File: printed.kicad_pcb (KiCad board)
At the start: 2 copper layers, 20.1 x 20.1 mm, 4 parts

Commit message: Netlist
Correctly Generated the letlist
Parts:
- removed 5050-2812B (x4): LED***, WS2812B
- added LED1: WS2812B, WS2812B, F.Cu at (162.6, 87.6)
- added LED2: WS2812B, WS2812B, F.Cu at (162.6, 95.2)
- added LED3: WS2812B, WS2812B, F.Cu at (170.2, 87.6)
- added LED4: WS2812B, WS2812B, F.Cu at (170.2, 95.2)
- added P1: CONN_4, 4P-Header, F.Cu at (160.0, 87.6)
- added P2: CONN_4, 4P-Header, F.Cu at (177.8, 87.6)
- added SIL-4: Val**, SIL-4, F.Cu at (0.00, 0.00)

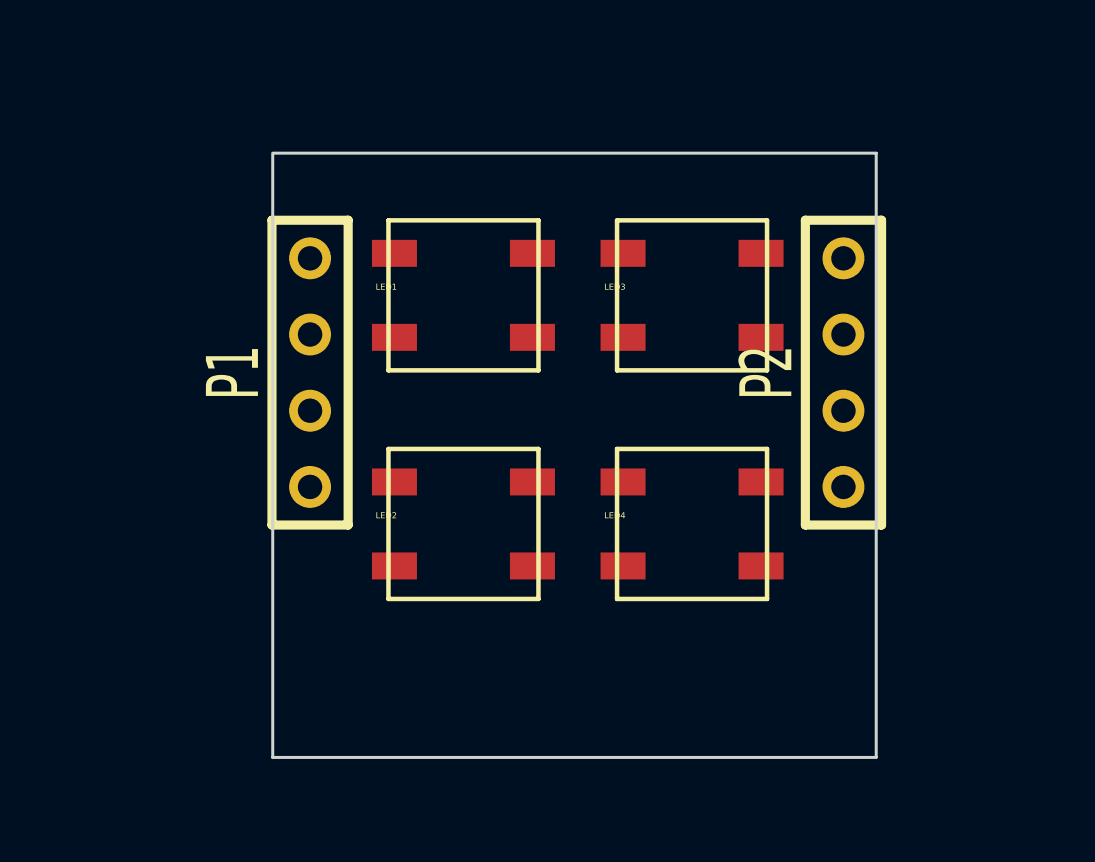
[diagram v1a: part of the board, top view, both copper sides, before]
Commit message: ws2812b schematic file
missed exporting the file
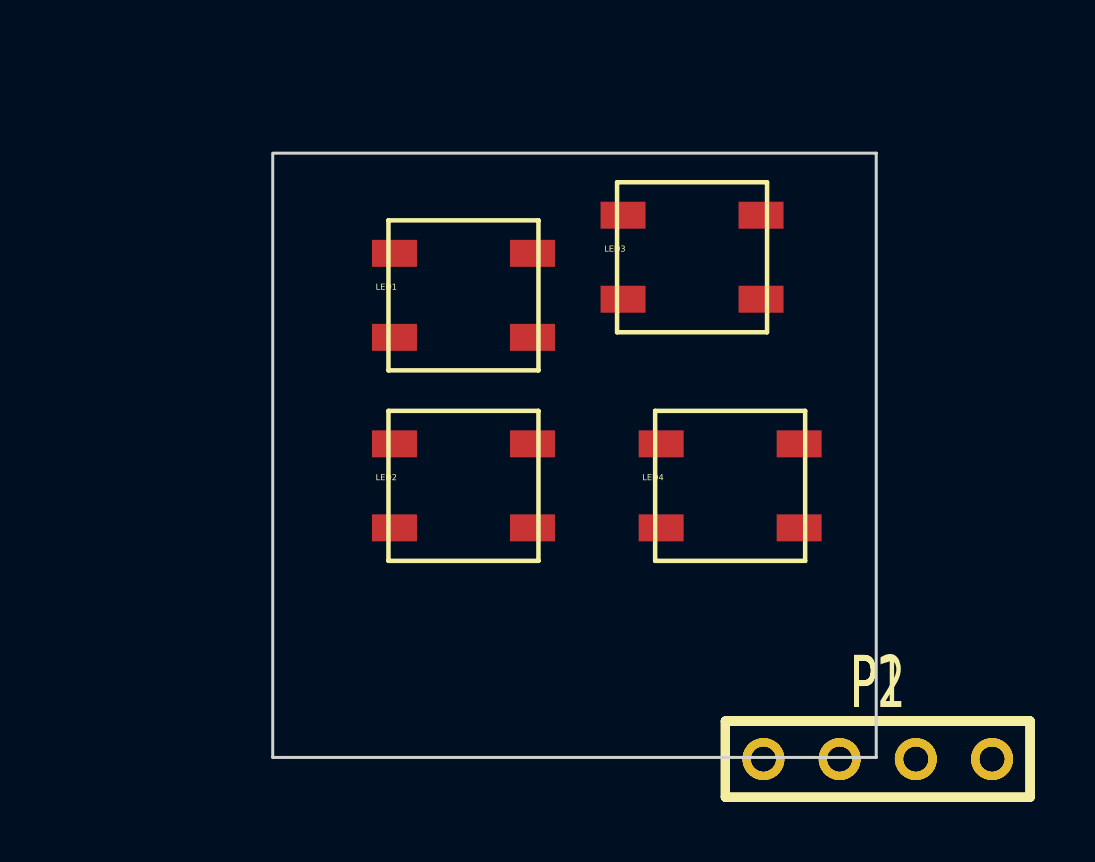
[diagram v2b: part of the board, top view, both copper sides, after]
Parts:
- moved P1 22.9 mm to (178.9, 100.5), turned to 0 degrees
- moved P2 12.9 mm to (178.9, 100.5), turned to 0 degrees
- moved LED4 1.80 mm to (171.4, 94.0)
- moved LED2 1.27 mm to (162.6, 94.0)
- moved LED3 1.27 mm to (170.2, 86.4)
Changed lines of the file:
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@@
   )
   (module WS2812B (layer Front.Layer)
-    (at 170.18 87.63)
+    (at 170.18 86.36)
     (descr "SMT 5050 WD2812")
     (fp_text reference LED3 (at 0 -2.8575) (layer F.SilkS)
@@
   )
   (module WS2812B (layer Front.Layer)
-    (at 162.56 95.25)
+    (at 162.56 93.98)
     (descr "SMT 5050 WD2812")
     (fp_text reference LED2 (at 0 -2.8575) (layer F.SilkS)
@@
   )
   (module WS2812B (layer Front.Layer)
-    (at 170.18 95.25)
+    (at 171.45 93.98)
     (descr "SMT 5050 WD2812")
     (fp_text reference LED4 (at 0 -2.8575) (layer F.SilkS)
@@
   )
   (module 4P-Header (layer Front.Layer)
-    (at 177.8 87.63 90)
+    (at 178.942201 100.512001)
     (descr "Connecteur 4 pibs")
     (tags "CONN DEV")
-    (fp_text reference P2 (at 0 -2.54 90) (layer F.SilkS)
+    (fp_text reference P2 (at 0 -2.54) (layer F.SilkS)
       (effects (font (size 1.73482 1.08712) (thickness 0.3048)))
     )
-    (fp_text value CONN_4 (at 0 -2.54 90) (layer F.SilkS) hide
+    (fp_text value CONN_4 (at 0 -2.54) (layer F.SilkS) hide
       (effects (font (size 1.524 1.016) (thickness 0.3048)))
     )
@@
     (fp_line (start 5.08 -1.27) (end 5.08 1.27) (layer F.SilkS) (width 0.3048))
     (fp_line (start 5.08 1.27) (end -5.08 1.27) (layer F.SilkS) (width 0.3048))
-    (pad 1 thru_hole circle (at -3.81 0 90) (size 1.397 1.397) (drill 0.8128)
+    (pad 1 thru_hole circle (at -3.81 0) (size 1.397 1.397) (drill 0.8128)
       (layers *.Cu *.Mask F.SilkS)
       (net 3 N-000002)
     )
-    (pad 2 thru_hole circle (at -1.27 0 90) (size 1.397 1.397) (drill 0.8128)
+    (pad 2 thru_hole circle (at -1.27 0) (size 1.397 1.397) (drill 0.8128)
       (layers *.Cu *.Mask F.SilkS)
       (net 9 N-000008)
     )
-    (pad 3 thru_hole circle (at 1.27 0 90) (size 1.397 1.397) (drill 0.8128)
+    (pad 3 thru_hole circle (at 1.27 0) (size 1.397 1.397) (drill 0.8128)
       (layers *.Cu *.Mask F.SilkS)
       (net 8 N-000007)
     )
-    (pad 4 thru_hole circle (at 3.81 0 90) (size 1.397 1.397) (drill 0.8128)
+    (pad 4 thru_hole circle (at 3.81 0) (size 1.397 1.397) (drill 0.8128)
       (layers *.Cu *.Mask F.SilkS)
       (net 4 N-000003)
@@
   )
   (module 4P-Header (layer Front.Layer)
-    (at 160.02 87.63 90)
+    (at 178.942201 100.512001)
     (descr "Connecteur 4 pibs")
     (tags "CONN DEV")
-    (fp_text reference P1 (at 0 -2.54 90) (layer F.SilkS)
+    (fp_text reference P1 (at 0 -2.54) (layer F.SilkS)
       (effects (font (size 1.73482 1.08712) (thickness 0.3048)))
     )
-    (fp_text value CONN_4 (at 0 -2.54 90) (layer F.SilkS) hide
+    (fp_text value CONN_4 (at 0 -2.54) (layer F.SilkS) hide
       (effects (font (size 1.524 1.016) (thickness 0.3048)))
     )
@@
     (fp_line (start 5.08 -1.27) (end 5.08 1.27) (layer F.SilkS) (width 0.3048))
     (fp_line (start 5.08 1.27) (end -5.08 1.27) (layer F.SilkS) (width 0.3048))
-    (pad 1 thru_hole circle (at -3.81 0 90) (size 1.397 1.397) (drill 0.8128)
+    (pad 1 thru_hole circle (at -3.81 0) (size 1.397 1.397) (drill 0.8128)
       (layers *.Cu *.Mask F.SilkS)
       (net 7 N-000006)
     )
-    (pad 2 thru_hole circle (at -1.27 0 90) (size 1.397 1.397) (drill 0.8128)
+    (pad 2 thru_hole circle (at -1.27 0) (size 1.397 1.397) (drill 0.8128)
       (layers *.Cu *.Mask F.SilkS)
       (net 6 N-000005)
     )
-    (pad 3 thru_hole circle (at 1.27 0 90) (size 1.397 1.397) (drill 0.8128)
+    (pad 3 thru_hole circle (at 1.27 0) (size 1.397 1.397) (drill 0.8128)
       (layers *.Cu *.Mask F.SilkS)
       (net 5 N-000004)
     )
-    (pad 4 thru_hole circle (at 3.81 0 90) (size 1.397 1.397) (drill 0.8128)
+    (pad 4 thru_hole circle (at 3.81 0) (size 1.397 1.397) (drill 0.8128)
       (layers *.Cu *.Mask F.SilkS)
       (net 2 N-0000010)

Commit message: Headers Added
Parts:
- removed SIL-4: Val**, SIL-4
- added P3: CONN_1, 1pin, F.Cu at (174.2, 96.2)
- added P4: CONN_1, 1pin, F.Cu at (165.9, 96.3)
- moved P2 24.5 mm to (158.2, 87.6), turned to 90 degrees
- moved P1 12.8 mm to (177.6, 87.7), turned to 90 degrees
- moved LED4 2.34 mm to (169.3, 93.2)
- moved LED1 1.98 mm to (160.7, 86.9)
- moved LED2 1.91 mm to (160.8, 93.3)
- moved LED3 0.99 mm to (169.3, 86.8)

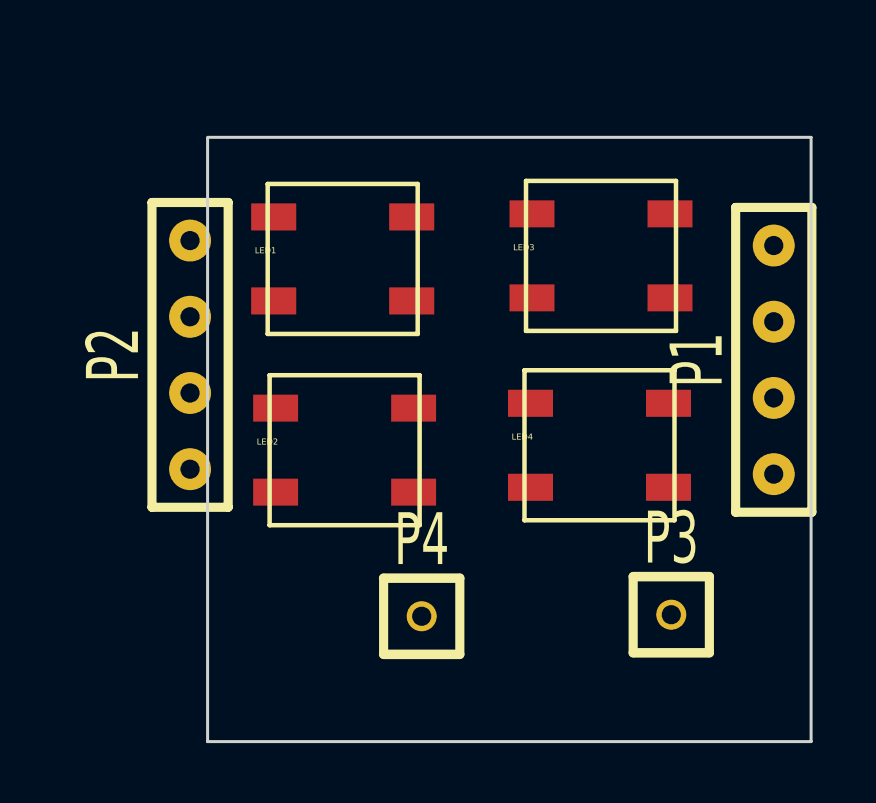
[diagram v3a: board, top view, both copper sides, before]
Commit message: Layout Change
TODO make even and smaller board
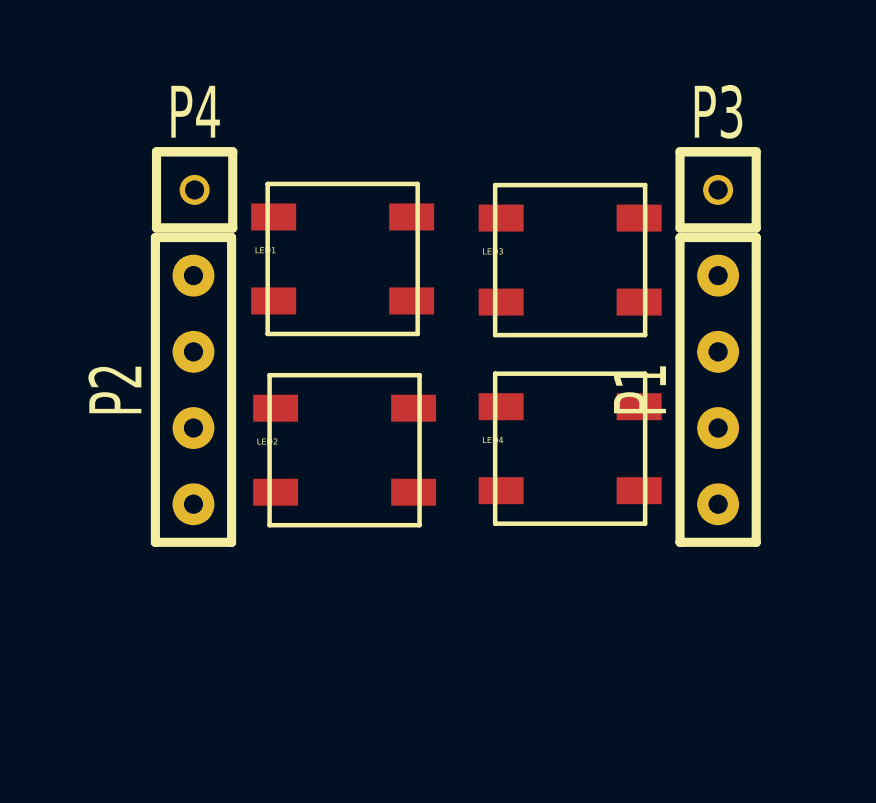
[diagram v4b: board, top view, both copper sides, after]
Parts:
- moved P4 16.1 mm to (158.3, 82.1)
- moved P3 14.2 mm to (175.8, 82.1)
- moved P1 2.11 mm to (175.8, 88.7)
- moved P2 1.17 mm to (158.3, 88.7)
- moved LED3 1.04 mm to (168.3, 87.0)
- moved LED4 0.98 mm to (168.3, 93.3)
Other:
- board outline removed
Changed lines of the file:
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@@
     (links 16)
     (no_connects 16)
-    (area 158.725399 80.264799 178.942201 100.507001)
+    (area 154.37739 80.264799 179.324001 100.507001)
     (thickness 1.6)
-    (drawings 4)
+    (drawings 0)
     (tracks 0)
     (zones 0)
@@
   )
   (module WS2812B (layer Front.Layer)
-    (at 169.3164 86.8426)
+    (at 168.2877 86.9823)
     (descr "SMT 5050 WD2812")
     (fp_text reference LED3 (at 0 -2.8575) (layer F.SilkS)
@@
   )
   (module WS2812B (layer Front.Layer)
-    (at 169.2656 93.1545)
+    (at 168.2877 93.2688)
     (descr "SMT 5050 WD2812")
     (fp_text reference LED4 (at 0 -2.8575) (layer F.SilkS)
@@
   )
   (module 4P-Header (layer Front.Layer)
-    (at 158.1912 87.5665 90)
+    (at 158.3055 88.7349 90)
     (descr "Connecteur 4 pibs")
     (tags "CONN DEV")
@@
   )
   (module 4P-Header (layer Front.Layer)
-    (at 177.6476 87.7316 90)
+    (at 175.7934 88.7349 90)
     (descr "Connecteur 4 pibs")
     (tags "CONN DEV")
@@
   )
   (module 1pin (layer Front.Layer)
-    (at 165.9128 96.2787)
+    (at 158.3436 82.0674)
     (descr "Connecteurs 1 pin")
     (tags "CONN DEV")
@@
   )
   (module 1pin (layer Front.Layer)
-    (at 174.2313 96.2279)
+    (at 175.7934 82.0674)
     (descr "Connecteurs 1 pin")
     (tags "CONN DEV")
@@
     )
   )
-  (gr_line (start 158.7754 100.457) (end 158.7754 80.3656) (angle 90) (layer Edge.Cuts) (width 0.1))
-  (gr_line (start 178.8922 100.457) (end 158.7754 100.457) (angle 90) (layer Edge.Cuts) (width 0.1))
-  (gr_line (start 178.8922 80.3148) (end 178.8922 100.457) (angle 90) (layer Edge.Cuts) (width 0.1))
-  (gr_line (start 158.7754 80.3148) (end 178.8922 80.3148) (angle 90) (layer Edge.Cuts) (width 0.1))
 )

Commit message: Final Schematic,
Nearly to creating the gerber file
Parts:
- removed LED1, LED2, LED3, LED4: WS2812B, WS2812B
- removed P1, P2: CONN_4, 4P-Header
- removed P3, P4: CONN_1, 1pin
- added ?: , WS2812B, F.Cu at (199.9, 146.2)
- added ?: , WS2812B, F.Cu at (207.1, 146.2)
- added ?: , WS2812B, F.Cu at (199.9, 152.2)
- added ?: , WS2812B, F.Cu at (207.1, 152.2)
- added ?: , 4P-Header, F.Cu at (197.2, 147.9)
- added ?: , 4P-Header, F.Cu at (215.0, 147.9)
- added ?: , 1pin, F.Cu at (215.0, 141.2)
- added ?: , 1pin, F.Cu at (197.3, 141.2)
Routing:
- net N-000009: track 0.00 -> 35.8 mm, vias 0 -> 5
- net N-000005: track 0.00 -> 34.9 mm
- net N-000008: track 0.00 -> 12.3 mm, vias 0 -> 1
- net N-0000010: track 0.00 -> 11.5 mm, vias 0 -> 1
- net N-000004: track 0.00 -> 11.0 mm, vias 0 -> 1
- net N-000003: track 0.00 -> 10.8 mm
- net N-000006: track 0.00 -> 5.88 mm
- net N-000002: track 0.00 -> 3.73 mm
- net N-000001: track 0.00 -> 3.61 mm
- net N-000007: track 0.00 -> 3.38 mm
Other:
- board outline added: 20.7 x 13.6 mm
